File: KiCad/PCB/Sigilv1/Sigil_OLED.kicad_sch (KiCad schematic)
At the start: 12 parts, among them J2 INLAND 1.3" OLED HEADER (7-PI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, J3 BUZZER 2-PIN HEADER, J5 NEOPIXEL JEWEL 7 RGBW, SW1 UP (GPIO25, J11), SW2 DOWN (GPIO27, J9), SW3 LEFT (GPIO19, A12), SW4 RIGHT (GPIO21, A14), SW5 SELECT (GPIO32, J13), U1 REMOVABLE ESP32 DEVKIT / 2 x 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

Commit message: Sigil schematics: ring level shifter, DevKit socket footprint, piezo buzzer
- U2 74AHCT1G125 (SOT-23-5, C3 100 nF) buffers GPIO26 to 5 V ahead of R1.
- U1 gets Sigil.pretty/ESP32_DevKit_38_Socket_Row25.4mm from published
  Inland DevKit dimensions (2.54 mm pitch, 25.4 mm rows); needs a caliper check.
- J3 documented as a directly driven passive piezo.

Co-Authored-By: Claude Opus 5.5 <noreply@anthropic.com>
Claude-Session: https://claude.ai/code/session_01EuTMd98XaCZ1DRqGGQFyaV
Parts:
- added C3: 100nF, Capacitor_THT:C_Disc_D5.0mm_W2.5mm_P5.00mm, symbol Sigil:Capacitor
- added U2: 74AHCT1G125, Package_TO_SOT_SMD:SOT-23-5, symbol Sigil:74AHCT1G125
- U1: footprint (none) -> Sigil:ESP32_DevKit_38_Socket_Row25.4mm
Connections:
- net +5V: now also C3.1, U2.5 (VCC)
- net GND: now also C3.2, U2.1 (OE#), U2.3 (GND)
- net RING_DIN: now also U2.2 (A); no longer R1.1
- new net RING_DIN_5V: R1.1, U2.4 (Y)
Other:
- note added: "Adafruit NeoPixel Jewel 7, RGBW, powered from USB 5V (J1). 3.3 V data worked on the breadboard, but it is below spec, so 74AHCT1G125 (U2) buffers GPIO26 to 5 V logic, then R1 (330 ohm). C1 (470 uF, + to PWR) is the recommended bulk capacitor across PWR/GND at the ring. Full RGBW is ~80 mA per pixel (~560 mA total), more than USB supplies: firmware caps brightness at 48/255. Draws the status light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"
- note added: "C2 10 uF X7R on +3V3; C3 100 nF at U2."
- note added: "J3 is a 2-pin header (1 SIG, 2 GND) for the buzzer on leads. Owner: a cheap passive piezo disc, driven directly by GPIO33 (LEDC tone). A magnetic transducer would need a driver instead."
- note added: "SCHEMATIC REVIEW / RELEASE HOLDS 1. U1 uses A1-A19 / J1-J19 from SigilBackMarked.png (BACK view); never exchange row identities. 2. U1 footprint (Sigil.pretty) is from published Inland specs: 2.54 mm pitch, 25.4 mm rows, 55.0 x 27.5 mm. Caliper-check and test-fit before ordering. 3. Future footprint: two 1x19 female sockets, unmistakable A1/J1 marks; verify insertion from carrier component side. 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"
- note removed: "Adafruit NeoPixel Jewel 7, RGBW, powered from USB 5V (J1). 3.3 V data into 5 V pixels usually works; if it glitches, add a 74AHCT125 level shifter. R1 (300-500 ohm) sits at the ring. C1 (470 uF, + to PWR) is the recommended bulk capacitor across PWR/GND at the ring. Full RGBW is ~80 mA per pixel (~560 mA total), more than USB supplies: firmware caps brightness at 48/255. Draws the status light (L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"
- note removed: "C2: 10 uF ceramic (X5R/X7R, >= 10 V) on +3V3 beside J2/J4."
- note removed: "J3 is a 2-pin header (1 SIG, 2 GND) for the breadboard buzzer on flying leads. The load is unconfirmed: a passive piezo can be driven directly; a magnetic transducer needs a transistor driver and flyback diode (not on this board)."
- note removed: "SCHEMATIC REVIEW / RELEASE HOLDS 1. U1 uses A1-A19 / J1-J19 from SigilBackMarked.png (BACK view); never exchange row identities. 2. No DevKit footprint assigned: measure pitch, row spacing, outline, USB-C overhang, holes, socket height and keepouts. 3. Future footprint: two 1x19 female sockets, unmistakable A1/J1 marks; verify insertion from carrier component side. 4. Keep USB-C, BOOT and EN/rese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"

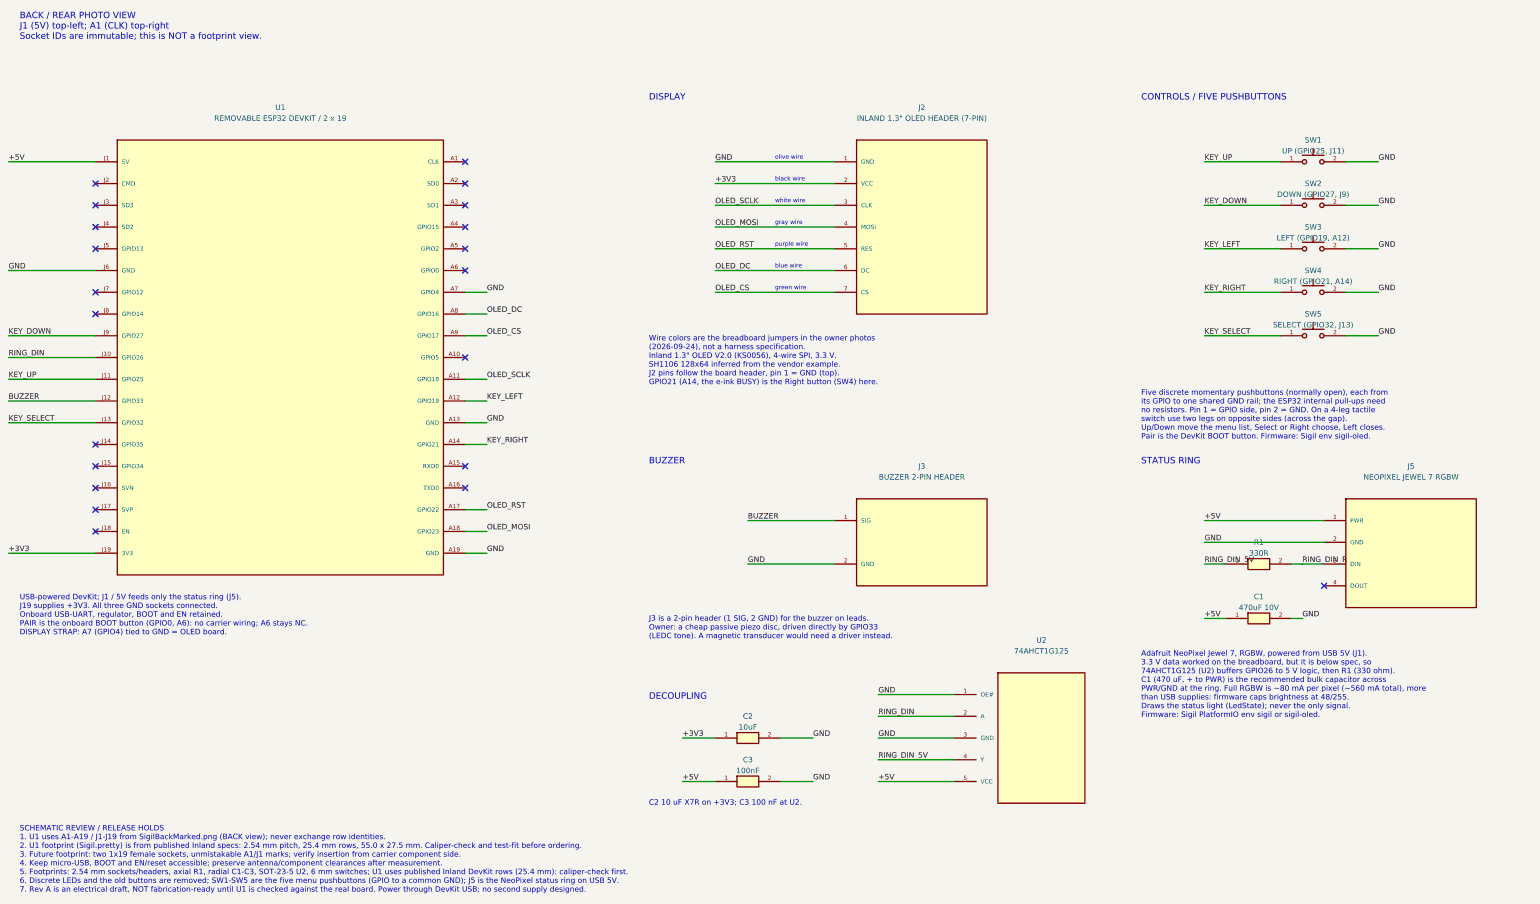
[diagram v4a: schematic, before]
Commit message: Jewel adapter board with a JST-XH pigtail into the Sigil board
- New Sigil_JewelAdapter project: pin holes at the Jewel 7 pad positions
  (from Adafruit's board file), its M2 holes, C1 470 uF, and holes for a
  3-wire JST-XH pigtail.
- Sigil boards: J5 becomes a JST-XH 3-pin socket (+5V, DIN, GND); C1 moves
  to the adapter. Verifier checks the adapter and that pin orders match.

Co-Authored-By: Claude Opus 5.5 <noreply@anthropic.com>
Claude-Session: https://claude.ai/code/session_01EuTMd98XaCZ1DRqGGQFyaV
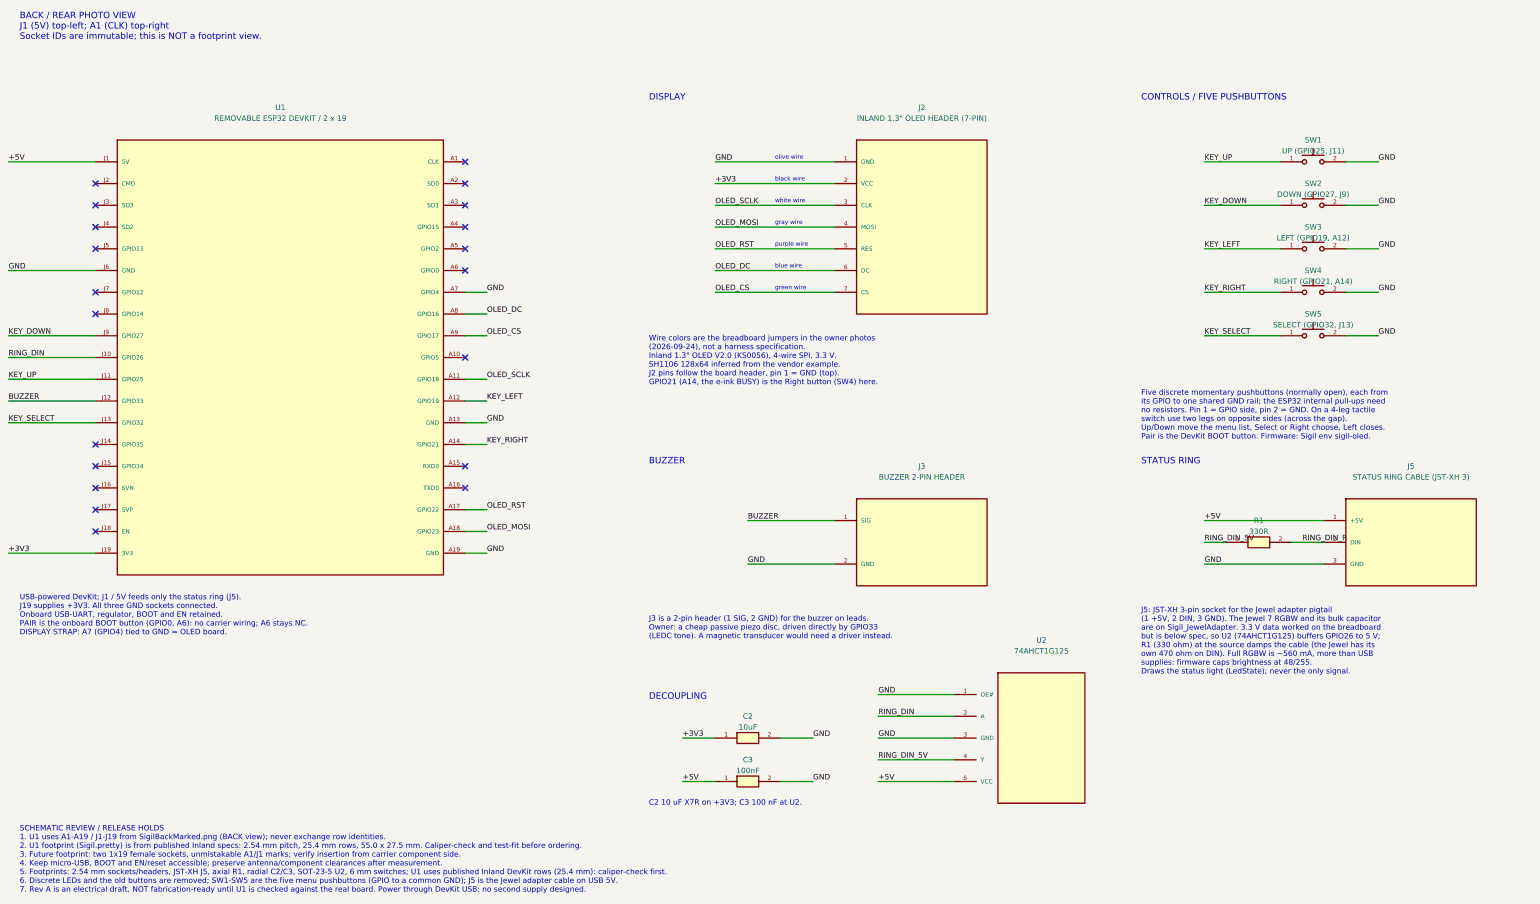
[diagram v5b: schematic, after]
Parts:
- removed C1: 470uF 10V, Capacitor_THT:CP_Radial_D8.0mm_P3.50mm, symbol Sigil:Capacitor
- J5: value NEOPIXEL JEWEL 7 RGBW -> STATUS RING CABLE (JST-XH 3); footprint Connector_PinHeader_2.54mm:PinHeader_1x04_P2.54mm_Vertical -> Connector_JST:JST_XH_B3B-XH-A_1x03_P2.50mm_Vertical; symbol Sigil:NeoPixel_Jewel7_RGBW -> Sigil:Ring_Cable_JST_XH_3
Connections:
- net GND: now also J5.3 (GND); no longer J5.2 (GND)
- net RING_DIN_R: now also J5.2 (DIN); no longer J5.3 (DIN)
- no-connect marks 21 -> 20
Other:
- note added: "J5: JST-XH 3-pin socket for the Jewel adapter pigtail (1 +5V, 2 DIN, 3 GND). The Jewel 7 RGBW and its bulk capacitor are on Sigil_JewelAdapter. 3.3 V data worked on the breadboard but is below spec, so U2 (74AHCT1G125) buffers GPIO26 to 5 V; R1 (330 ohm) at the source damps the cable (the Jewel has its own 470 ohm on DIN). Full RGBW is ~560 mA, more than USB supplies: firmware caps brightness at 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"
- note removed: "Adafruit NeoPixel Jewel 7, RGBW, powered from USB 5V (J1). 3.3 V data worked on the breadboard, but it is below spec, so 74AHCT1G125 (U2) buffers GPIO26 to 5 V logic, then R1 (330 ohm). C1 (470 uF, + to PWR) is the recommended bulk capacitor across PWR/GND at the ring. Full RGBW is ~80 mA per pixel (~560 mA total), more than USB supplies: firmware caps brightness at 48/255. Draws the status light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"
- moved on the sheet: R1
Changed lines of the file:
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@@
 (text "Five discrete momentary pushbuttons (normally open), each from\nits GPIO to one shared GND rail; the ESP32 internal pull-ups need\nno resistors. Pin 1 = GPIO side, pin 2 = GND. On a 4-leg tactile\nswitch use two legs on opposite sides (across the gap).\nUp/Down move the menu list, Select or Right choose, Left closes.\nPair is the DevKit BOOT button. Firmware: Sigil env sigil-oled." (at 290 109.22 0) (effects (font (size 1.27 1.27)) (justify left top)))
 (text "STATUS RING" (at 290 125 0) (effects (font (size 1.5 1.5)) (justify left top)))
-(symbol (lib_id "Sigil:NeoPixel_Jewel7_RGBW") (at 353.06 139.7 0) (unit 1) (in_bom yes) (on_board yes) (dnp no)
- (property "Reference" "J5" (at 353.06 126.99999999999999 0)  (effects (font (size 1.27 1.27))))(property "Value" "NEOPIXEL JEWEL 7 RGBW" (at 353.06 129.54 0)  (effects (font (size 1.27 1.27)))) (property "Footprint" "Connector_PinHeader_2.54mm:PinHeader_1x04_P2.54mm_Vertical" (at 353.06 139.7 0) (hide yes) (effects (font (size 1.27 1.27)))) (pin "1")(pin "2")(pin "3")(pin "4")
+(symbol (lib_id "Sigil:Ring_Cable_JST_XH_3") (at 353.06 139.7 0) (unit 1) (in_bom yes) (on_board yes) (dnp no)
+ (property "Reference" "J5" (at 353.06 126.99999999999999 0)  (effects (font (size 1.27 1.27))))(property "Value" "STATUS RING CABLE (JST-XH 3)" (at 353.06 129.54 0)  (effects (font (size 1.27 1.27)))) (property "Footprint" "Connector_JST:JST_XH_B3B-XH-A_1x03_P2.50mm_Vertical" (at 353.06 139.7 0) (hide yes) (effects (font (size 1.27 1.27)))) (pin "1")(pin "2")(pin "3")
       (instances (project "Sigil_OLED" (path "/a61c2f0e-3b7d-4e55-9c1a-5d0e7b8f2c41" (reference "J5") (unit 1)))))
 (wire (pts (xy 332.74 139.7) (xy 304.8 139.7)) (stroke (width 0) (type default)))
 (label "+5V" (at 304.8 139.7 0) (effects (font (size 1.27 1.27)) (justify left bottom)))
-(wire (pts (xy 332.74 144.78) (xy 304.8 144.78)) (stroke (width 0) (type default)))
-(label "GND" (at 304.8 144.78 0) (effects (font (size 1.27 1.27)) (justify left bottom)))
-(symbol (lib_id "Sigil:Resistor_Series") (at 317.5 149.86 0) (unit 1) (in_bom yes) (on_board yes) (dnp no)
- (property "Reference" "R1" (at 317.5 144.78 0)  (effects (font (size 1.27 1.27))))(property "Value" "330R" (at 317.5 147.32 0)  (effects (font (size 1.27 1.27)))) (property "Footprint" "Resistor_THT:R_Axial_DIN0207_L6.3mm_D2.5mm_P7.62mm_Horizontal" (at 317.5 149.86 0) (hide yes) (effects (font (size 1.27 1.27)))) (pin "1")(pin "2")
+(symbol (lib_id "Sigil:Resistor_Series") (at 317.5 144.78 0) (unit 1) (in_bom yes) (on_board yes) (dnp no)
+ (property "Reference" "R1" (at 317.5 139.7 0)  (effects (font (size 1.27 1.27))))(property "Value" "330R" (at 317.5 142.23999999999998 0)  (effects (font (size 1.27 1.27)))) (property "Footprint" "Resistor_THT:R_Axial_DIN0207_L6.3mm_D2.5mm_P7.62mm_Horizontal" (at 317.5 144.78 0) (hide yes) (effects (font (size 1.27 1.27)))) (pin "1")(pin "2")
       (instances (project "Sigil_OLED" (path "/a61c2f0e-3b7d-4e55-9c1a-5d0e7b8f2c41" (reference "R1") (unit 1)))))
-(wire (pts (xy 309.88 149.86) (xy 304.8 149.86)) (stroke (width 0) (type default)))
-(label "RING_DIN_5V" (at 304.8 149.86 0) (effects (font (size 1.27 1.27)) (justify left bottom)))
-(wire (pts (xy 325.12 149.86) (xy 327.66 149.86)) (stroke (width 0) (type default)))
-(wire (pts (xy 327.66 149.86) (xy 332.74 149.86)) (stroke (width 0) (type default)))
-(label "RING_DIN_R" (at 327.66 149.86 0) (effects (font (size 1.27 1.27)) (justify left bottom)))
-(no_connect (at 332.74 154.94))
-(symbol (lib_id "Sigil:Capacitor") (at 317.5 162.56 0) (unit 1) (in_bom yes) (on_board yes) (dnp no)
- (property "Reference" "C1" (at 317.5 157.48 0)  (effects (font (size 1.27 1.27))))(property "Value" "470uF 10V" (at 317.5 160.01999999999998 0)  (effects (font (size 1.27 1.27)))) (property "Footprint" "Capacitor_THT:CP_Radial_D8.0mm_P3.50mm" (at 317.5 162.56 0) (hide yes) (effects (font (size 1.27 1.27)))) (pin "1")(pin "2")
-      (instances (project "Sigil_OLED" (path "/a61c2f0e-3b7d-4e55-9c1a-5d0e7b8f2c41" (reference "C1") (unit 1)))))
-(wire (pts (xy 309.88 162.56) (xy 304.8 162.56)) (stroke (width 0) (type default)))
-(label "+5V" (at 304.8 162.56 0) (effects (font (size 1.27 1.27)) (justify left bottom)))
-(wire (pts (xy 325.12 162.56) (xy 327.66 162.56)) (stroke (width 0) (type default)))
-(label "GND" (at 327.66 162.56 0) (effects (font (size 1.27 1.27)) (justify left bottom)))
-(text "Adafruit NeoPixel Jewel 7, RGBW, powered from USB 5V (J1).\n3.3 V data worked on the breadboard, but it is below spec, so\n74AHCT1G125 (U2) buffers GPIO26 to 5 V logic, then R1 (330 ohm).\nC1 (470 uF, + to PWR) is the recommended bulk capacitor across\nPWR/GND at the ring. Full RGBW is ~80 mA per pixel (~560 mA total), more\nthan USB supplies: firmware caps brightness at 48/255.\nDraws the status light (LedState); never the only signal.\nFirmware: Sigil PlatformIO env sigil or sigil-oled." (at 290 170.18 0) (effects (font (size 1.27 1.27)) (justify left top)))
-(text "SCHEMATIC REVIEW / RELEASE HOLDS\n1. U1 uses A1-A19 / J1-J19 from SigilBackMarked.png (BACK view); never exchange row identities.\n2. U1 footprint (Sigil.pretty) is from published Inland specs: 2.54 mm pitch, 25.4 mm rows, 55.0 x 27.5 mm. Caliper-check and test-fit before ordering.\n3. Future footprint: two 1x19 female sockets, unmistakable A1/J1 marks; verify insertion from carrier component side.\n4. Keep micro-USB, BOOT and EN/reset accessible; preserve antenna/component clearances after measurement.\n5. Footprints: 2.54 mm sockets/headers, axial R1, radial C1-C3, SOT-23-5 U2, 6 mm switches; U1 uses published Inland DevKit rows (25.4 mm): caliper-check first.\n6. Discrete LEDs and the old buttons are removed; SW1-SW5 are the five menu pushbuttons (GPIO to a common GND); J5 is the NeoPixel status ring on USB 5V.\n7. Rev A is an electrical draft, NOT fabrication-ready until U1 is checked against the real board. Power through DevKit USB; no second supply designed." (at 28 211 0) (effects (font (size 1.27 1.27)) (justify left top)))
+(wire (pts (xy 309.88 144.78) (xy 304.8 144.78)) (stroke (width 0) (type default)))
+(label "RING_DIN_5V" (at 304.8 144.78 0) (effects (font (size 1.27 1.27)) (justify left bottom)))
+(wire (pts (xy 325.12 144.78) (xy 327.66 144.78)) (stroke (width 0) (type default)))
+(wire (pts (xy 327.66 144.78) (xy 332.74 144.78)) (stroke (width 0) (type default)))
+(label "RING_DIN_R" (at 327.66 144.78 0) (effects (font (size 1.27 1.27)) (justify left bottom)))
+(wire (pts (xy 332.74 149.86) (xy 304.8 149.86)) (stroke (width 0) (type default)))
+(label "GND" (at 304.8 149.86 0) (effects (font (size 1.27 1.27)) (justify left bottom)))
+(text "J5: JST-XH 3-pin socket for the Jewel adapter pigtail\n(1 +5V, 2 DIN, 3 GND). The Jewel 7 RGBW and its bulk capacitor\nare on Sigil_JewelAdapter. 3.3 V data worked on the breadboard\nbut is below spec, so U2 (74AHCT1G125) buffers GPIO26 to 5 V;\nR1 (330 ohm) at the source damps the cable (the Jewel has its\nown 470 ohm on DIN). Full RGBW is ~560 mA, more than USB\nsupplies: firmware caps brightness at 48/255.\nDraws the status light (LedState); never the only signal." (at 290 160.02 0) (effects (font (size 1.27 1.27)) (justify left top)))
+(text "SCHEMATIC REVIEW / RELEASE HOLDS\n1. U1 uses A1-A19 / J1-J19 from SigilBackMarked.png (BACK view); never exchange row identities.\n2. U1 footprint (Sigil.pretty) is from published Inland specs: 2.54 mm pitch, 25.4 mm rows, 55.0 x 27.5 mm. Caliper-check and test-fit before ordering.\n3. Future footprint: two 1x19 female sockets, unmistakable A1/J1 marks; verify insertion from carrier component side.\n4. Keep micro-USB, BOOT and EN/reset accessible; preserve antenna/component clearances after measurement.\n5. Footprints: 2.54 mm sockets/headers, JST-XH J5, axial R1, radial C2/C3, SOT-23-5 U2, 6 mm switches; U1 uses published Inland DevKit rows (25.4 mm): caliper-check first.\n6. Discrete LEDs and the old buttons are removed; SW1-SW5 are the five menu pushbuttons (GPIO to a common GND); J5 is the Jewel adapter cable on USB 5V.\n7. Rev A is an electrical draft, NOT fabrication-ready until U1 is checked against the real board. Power through DevKit USB; no second supply designed." (at 28 211 0) (effects (font (size 1.27 1.27)) (justify left top)))
 (embedded_fonts no))
